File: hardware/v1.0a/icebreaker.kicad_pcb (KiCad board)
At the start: 4 copper layers, 73 x 37 mm, 124 parts, among them J1 Jumper, J10 Jumper, J11 Jumper, J12 Jumper, J13 Jumper, J14 Jumper, J15 Jumper, J16 Jumper, J17 Jumper, J18 Jumper, J19 Jumper, J2 Jumper, J20 Flash, J21 PMOD_1A, J22 PMOD_1B, J23 PMOD_2H, J24 PMOD_2P, J25 RGB Led, J26 5V AUX, J27 5V AUX, J3 Jumper, J4 Jumper, J5 Jumper, J6 Jumper, J7 Jumper, J8 Jumper, J9 Jumper, P1 pkl_USB_OTG, P2 UP, P3 UP, P4 UP, P5 UP, SW1 TACT, SW2 TACT, SW3 TACT, SW4 TACT, U1 93C46B-SOT-23-6, U2 3.3V, U3 1V2, U4 FT2232H, U5 W25Q, U6 ICE5LP4K-SG48, U7 12MHz

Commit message: Use normally closed jumpers. And fix VCCIO2 bypass. Closes #11
These jumpers connect two nets without impacting the schematic net
lists. This is a safer solution and easier to read than having to
remember where the net jumpers have to go and not miss a side path.
These jumpers use a hack of KiCAD where the DRC ignores lines on the
copper layer in footprints. The two pads of the jumper are shorted
within the footprint but they are not from the perspective of the DRC.
While I was already at it I have also replaced / separator with |
separator for multifunction nets. Unfortunately KiCAD reserves the /
separator for its multisheet net naming. This patch should fix the
bypass of the VCCIO0 jumper that was a mistake in the previous versions
of the board.
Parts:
- added REF**: 1b2_Logo_SilkS_5mm, pkl_logos:1b2_Logo_SilkS_5mm, B.Cu at (42.2, 47.2)
- J1, J15, J16, J18, J2: footprint pkl_jumpers:J_0603 -> pkl_jumpers:J_NC_0603_15
- J14, J17, J19: footprint pkl_jumpers:J_0603 -> pkl_jumpers:J_NC_0603_30
- turned J17 to 135 degrees
- turned J19 to 45 degrees
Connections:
- net Net-(C24-Pad1) renamed /VCCPLL
- C23 pad 1: +1V2 -> /VCORE
- C25 pad 1: +1V2 -> /VCORE
- C27 pad 2: +3V3 -> /VCCIO_2
- C28 pad 1: +1V2 -> /VCORE
- C30 pad 1: +3V3 -> /VCCIO_0|1
- C31 pad 1: +3V3 -> /VCCIO_0|1
- C36 pad 1: +1V2 -> /VCORE
- C37 pad 1: +1V2 -> /VCORE
- C38 pad 1: +1V2 -> /VCORE
- J1 pad 1: /Rx_TTL|FIFO_D0 -> /xFIFO_D0
- J14 pad 1: +1V2 -> /VCORE
- J15 pad 2: /FLASH_MOSI|IO0 -> /iCE_MISO
- J16 pad 1: /FLASH_MISO|IO1 -> /iCE_MOSI
- J17 pad 1: +3V3 -> /VCCIO_2
- J18 pad 1: /iCE_SS_B -> /FLASH_CS
- J19 pad 1: +3V3 -> /VCCIO_0|1
- J2 pad 1: /Tx_TTL|FIFO_D1 -> /xFIFO_D1
- J20 pad 1: /iCE_SS_B -> /FLASH_CS
- R10 pad 2: +1V2 -> /VCORE
- R11 pad 6: /iCE_SS_B -> /FLASH_CS
- U4 pad 38: /Rx_TTL|FIFO_D0 -> /xFIFO_D0
- U4 pad 39: /Tx_TTL|FIFO_D1 -> /xFIFO_D1
- U5 pad 1: /iCE_SS_B -> /FLASH_CS
- U6 pad 1: +3V3 -> /VCCIO_2
- U6 pad 14: /FLASH_MOSI|IO0 -> /iCE_MISO
- U6 pad 17: /FLASH_MISO|IO1 -> /iCE_MOSI
- U6 pad 22: +3V3 -> /VCCIO_0|1
- U6 pad 30: +1V2 -> /VCORE
- U6 pad 33: +3V3 -> /VCCIO_0|1
- U6 pad 5: +1V2 -> /VCORE
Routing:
- net +1V2: track 47.5 -> 18.4 mm, vias 4 -> 1
- net /VCORE: track 0.00 -> 27.9 mm, vias 0 -> 3
- net /iCE_SS_B: track 61.4 -> 34.5 mm, vias 3 -> 2
- net /FLASH_CS: track 0.00 -> 25.8 mm, vias 0 -> 1
- net +3V3: track 94.7 -> 69.5 mm, vias 35 -> 32
- net /VCCIO_0|1: track 0.00 -> 18.3 mm, vias 0 -> 2
- net /Rx_TTL|FIFO_D0: track 19.6 -> 7.27 mm, vias 2 -> 1
- net /xFIFO_D0: track 0.00 -> 11.1 mm, vias 0 -> 1
- net /FLASH_MISO|IO1: track 51.3 -> 40.2 mm, vias 3 -> 2
- net /FLASH_MOSI|IO0: track 51.4 -> 40.4 mm, vias 3 -> 2
- net /iCE_MOSI: track 0.00 -> 9.90 mm, vias 0 -> 1
- net /iCE_MISO: track 0.00 -> 9.79 mm, vias 0 -> 1
- net /Tx_TTL|FIFO_D1: track 17.7 -> 9.84 mm, vias 2 -> 1
- net /xFIFO_D1: track 0.00 -> 6.70 mm, vias 0 -> 1
- net /VCCIO_2: track 0.00 -> 4.55 mm, vias 0 -> 1

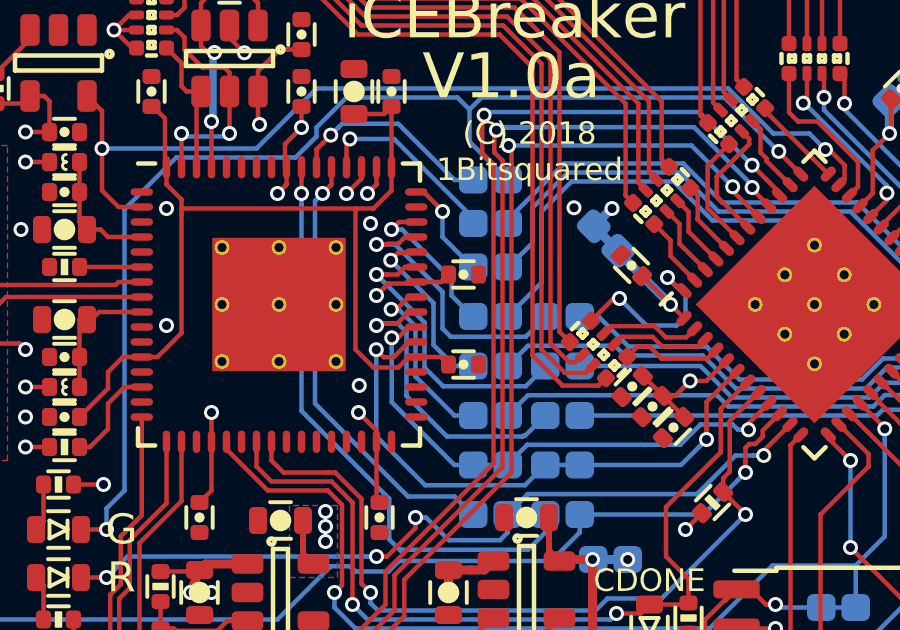
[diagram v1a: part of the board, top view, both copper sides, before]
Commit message: Added pulldown on the B port ~CTS ftdi line. Closes #10
With this line pulled down we can use minicom even when hardware flow
control is enabled. If this pin is not pulled low and hardware flow
control is used, no data is ever sent out by the FTDI chip. This can
easily happen because minicom has hardware flow control enabled by
default.

I decided to only add the CTS line pulldown to keep the placements under
control.
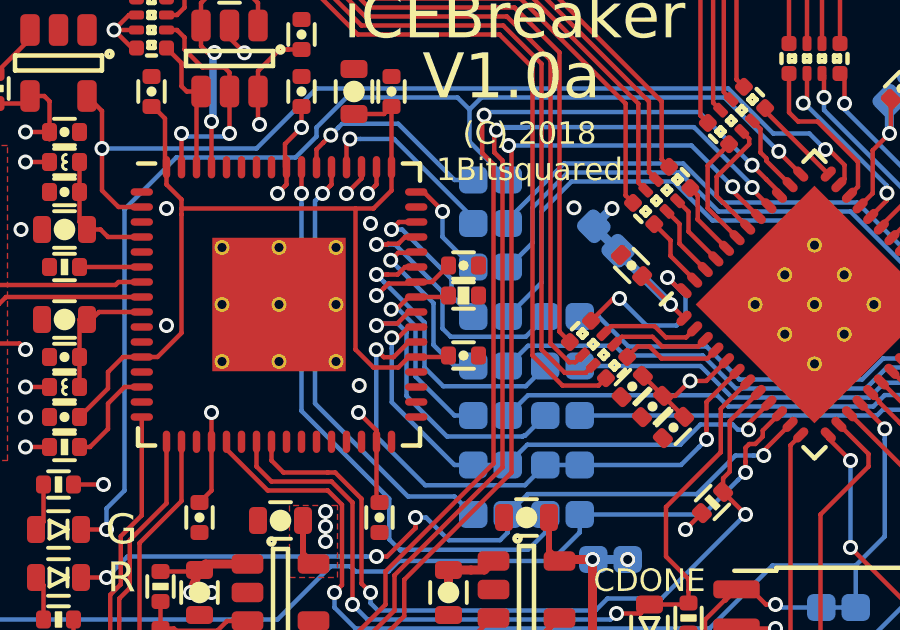
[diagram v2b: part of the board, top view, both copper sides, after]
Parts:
- added R25: 10k, pkl_dipol:R_0402, F.Cu at (50.5, 47.2)
- moved C16 0.30 mm to (50.5, 49.2)
- moved C20 0.30 mm to (50.5, 46.2)
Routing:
- net /xFIFO_D3: track 6.19 -> 7.29 mm
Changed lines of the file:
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@@
     (thickness 1.6)
     (drawings 143)
-    (tracks 1396)
+    (tracks 1398)
     (zones 0)
-    (modules 125)
+    (modules 126)
     (nets 133)
   )
@@
     (add_net "Net-(U7-Pad2)")
   )
+  (module pkl_dipol:R_0402 (layer F.Cu)
+    (at 50.5 47.2)
+    (descr "Resistor SMD 0402, reflow soldering")
+    (tags "resistor 0402")
+    (attr smd)
+    (fp_text reference R25 (at 0 0) (layer F.Fab)
+      (effects (font (size 0.635 0.635) (thickness 0.1)))
+    )
+    (fp_text value 10k (at 1.9 0) (layer F.Fab)
+      (effects (font (size 0.635 0.635) (thickness 0.1)))
+    )
+    (fp_poly (pts (xy -0.175 0.275) (xy -0.175 -0.275) (xy 0.175 -0.275) (xy 0.175 0.275)
+      (xy -0.1 0.275)) (layer F.SilkS) (width 0.05))
+    (fp_line (start -0.95 -0.5) (end 0.95 -0.5) (layer F.CrtYd) (width 0.05))
+    (fp_line (start -0.95 0.5) (end 0.95 0.5) (layer F.CrtYd) (width 0.05))
+    (fp_line (start -0.95 -0.5) (end -0.95 0.5) (layer F.CrtYd) (width 0.05))
+    (fp_line (start 0.95 -0.5) (end 0.95 0.5) (layer F.CrtYd) (width 0.05))
+    (fp_line (start -0.35 -0.44) (end 0.35 -0.44) (layer F.SilkS) (width 0.13))
+    (fp_line (start 0.35 0.44) (end -0.35 0.44) (layer F.SilkS) (width 0.13))
+    (pad 1 smd roundrect (at -0.5 0) (size 0.5 0.6) (layers F.Cu F.Paste F.Mask) (roundrect_rratio 0.25)
+      (net 21 /xFIFO_D3))
+    (pad 2 smd roundrect (at 0.5 0) (size 0.5 0.6) (layers F.Cu F.Paste F.Mask) (roundrect_rratio 0.25)
+      (net 26 GND))
+    (model ${KISYS3DMOD}/Resistor_SMD.3dshapes/R_0402_1005Metric.step
+      (at (xyz 0 0 0))
+      (scale (xyz 1 1 1))
+      (rotate (xyz 0 0 0))
+    )
+  )
   (module pkl_jumpers:J_NC_0603_15 (layer B.Cu)
     (at 53.8 52.85)
@@
   )
   (module pkl_dipol:C_0402 (layer F.Cu)
-    (at 50.5 49.5)
+    (at 50.5 49.2)
     (descr "Capacitor SMD 0402, reflow soldering")
     (tags "capacitor 0402")
@@
       (effects (font (size 0.635 0.635) (thickness 0.1)))
     )
-    (fp_text value 100n (at 0.2 1.2) (layer F.Fab)
+    (fp_text value 100n (at 0.2 1) (layer F.Fab)
       (effects (font (size 0.635 0.635) (thickness 0.1)))
     )
-    (fp_circle (center 0 0) (end 0 -0.085) (layer F.SilkS) (width 0.17))
-    (fp_line (start -0.95 -0.5) (end 0.95 -0.5) (layer F.CrtYd) (width 0.05))
-    (fp_line (start -0.95 0.5) (end 0.95 0.5) (layer F.CrtYd) (width 0.05))
-    (fp_line (start -0.95 -0.5) (end -0.95 0.5) (layer F.CrtYd) (width 0.05))
-    (fp_line (start 0.95 -0.5) (end 0.95 0.5) (layer F.CrtYd) (width 0.05))
-    (fp_line (start -0.35 -0.44) (end 0.35 -0.44) (layer F.SilkS) (width 0.13))
     (fp_line (start 0.35 0.44) (end -0.35 0.44) (layer F.SilkS) (width 0.13))
-    (pad 1 smd roundrect (at -0.5 0) (size 0.5 0.6) (layers F.Cu F.Paste F.Mask) (roundrect_rratio 0.25)
-      (net 39 +1V8))
+    (fp_line (start -0.35 -0.44) (end 0.35 -0.44) (layer F.SilkS) (width 0.13))
+    (fp_line (start 0.95 -0.5) (end 0.95 0.5) (layer F.CrtYd) (width 0.05))
+    (fp_line (start -0.95 -0.5) (end -0.95 0.5) (layer F.CrtYd) (width 0.05))
+    (fp_line (start -0.95 0.5) (end 0.95 0.5) (layer F.CrtYd) (width 0.05))
+    (fp_line (start -0.95 -0.5) (end 0.95 -0.5) (layer F.CrtYd) (width 0.05))
+    (fp_circle (center 0 0) (end 0 -0.085) (layer F.SilkS) (width 0.17))
     (pad 2 smd roundrect (at 0.5 0) (size 0.5 0.6) (layers F.Cu F.Paste F.Mask) (roundrect_rratio 0.25)
       (net 26 GND))
+    (pad 1 smd roundrect (at -0.5 0) (size 0.5 0.6) (layers F.Cu F.Paste F.Mask) (roundrect_rratio 0.25)
+      (net 39 +1V8))
     (model ${KISYS3DMOD}/Capacitor_SMD.3dshapes/C_0402_1005Metric.step
       (at (xyz 0 0 0))
@@
   )
   (module pkl_dipol:C_0402 (layer F.Cu)
-    (at 50.5 46.5)
+    (at 50.5 46.2)
     (descr "Capacitor SMD 0402, reflow soldering")
     (tags "capacitor 0402")
@@
       (effects (font (size 0.635 0.635) (thickness 0.1)))
     )
-    (fp_text value 100n (at 0.2 1) (layer F.Fab)
+    (fp_text value 100n (at 2.2 0) (layer F.Fab)
       (effects (font (size 0.635 0.635) (thickness 0.1)))
     )
-    (fp_circle (center 0 0) (end 0 -0.085) (layer F.SilkS) (width 0.17))
-    (fp_line (start -0.95 -0.5) (end 0.95 -0.5) (layer F.CrtYd) (width 0.05))
-    (fp_line (start -0.95 0.5) (end 0.95 0.5) (layer F.CrtYd) (width 0.05))
-    (fp_line (start -0.95 -0.5) (end -0.95 0.5) (layer F.CrtYd) (width 0.05))
-    (fp_line (start 0.95 -0.5) (end 0.95 0.5) (layer F.CrtYd) (width 0.05))
-    (fp_line (start -0.35 -0.44) (end 0.35 -0.44) (layer F.SilkS) (width 0.13))
     (fp_line (start 0.35 0.44) (end -0.35 0.44) (layer F.SilkS) (width 0.13))
-    (pad 1 smd roundrect (at -0.5 0) (size 0.5 0.6) (layers F.Cu F.Paste F.Mask) (roundrect_rratio 0.25)
-      (net 3 +3V3))
+    (fp_line (start -0.35 -0.44) (end 0.35 -0.44) (layer F.SilkS) (width 0.13))
+    (fp_line (start 0.95 -0.5) (end 0.95 0.5) (layer F.CrtYd) (width 0.05))
+    (fp_line (start -0.95 -0.5) (end -0.95 0.5) (layer F.CrtYd) (width 0.05))
+    (fp_line (start -0.95 0.5) (end 0.95 0.5) (layer F.CrtYd) (width 0.05))
+    (fp_line (start -0.95 -0.5) (end 0.95 -0.5) (layer F.CrtYd) (width 0.05))
+    (fp_circle (center 0 0) (end 0 -0.085) (layer F.SilkS) (width 0.17))
     (pad 2 smd roundrect (at 0.5 0) (size 0.5 0.6) (layers F.Cu F.Paste F.Mask) (roundrect_rratio 0.25)
       (net 26 GND))
+    (pad 1 smd roundrect (at -0.5 0) (size 0.5 0.6) (layers F.Cu F.Paste F.Mask) (roundrect_rratio 0.25)
+      (net 3 +3V3))
     (model ${KISYS3DMOD}/Capacitor_SMD.3dshapes/C_0402_1005Metric.step
       (at (xyz 0 0 0))
@@
   (segment (start 32.4 59.1) (end 33.05 59.1) (width 0.15) (layer F.Cu) (net 3))
   (via (at 33.45 58.7) (size 0.5) (drill 0.3) (layers F.Cu B.Cu) (net 3))
-  (segment (start 49.75 46.75) (end 50 46.5) (width 0.15) (layer F.Cu) (net 3))
-  (segment (start 48.925 46.75) (end 49.75 46.75) (width 0.15) (layer F.Cu) (net 3))
+  (segment (start 49.45 46.75) (end 50 46.2) (width 0.15) (layer F.Cu) (net 3))
+  (segment (start 48.925 46.75) (end 49.45 46.75) (width 0.15) (layer F.Cu) (net 3))
   (segment (start 64.541475 51.998135) (end 64.541475 51.644582) (width 0.15) (layer B.Cu) (net 4))
   (segment (start 64.541475 51.609242) (end 64.541475 51.644582) (width 0.15) (layer F.Cu) (net 4))
@@
   (segment (start 48.925 47.25) (end 48.675 47.25) (width 0.15) (layer F.Cu) (net 21))
   (segment (start 48.675 47.25) (end 48.264647 47.660353) (width 0.15) (layer F.Cu) (net 21))
+  (segment (start 49.95 47.25) (end 50 47.2) (width 0.15) (layer F.Cu) (net 21))
+  (segment (start 48.925 47.25) (end 49.95 47.25) (width 0.15) (layer F.Cu) (net 21))
   (segment (start 49.95 51.9) (end 52.475722 51.9) (width 0.15) (layer B.Cu) (net 22))
   (segment (start 52.550011 51.874989) (end 53.225 51.2) (width 0.15) (layer B.Cu) (net 22))
@@
   (segment (start 37.7 51.25) (end 38.65 50.3) (width 0.15) (layer F.Cu) (net 39))
   (segment (start 39.15 49.25) (end 39.775 49.25) (width 0.15) (layer F.Cu) (net 39))
-  (segment (start 49.75 49.25) (end 50 49.5) (width 0.15) (layer F.Cu) (net 39))
-  (segment (start 48.925 49.25) (end 49.75 49.25) (width 0.15) (layer F.Cu) (net 39))
+  (segment (start 49.95 49.25) (end 50 49.2) (width 0.15) (layer F.Cu) (net 39))
+  (segment (start 48.925 49.25) (end 49.95 49.25) (width 0.15) (layer F.Cu) (net 39))
   (segment (start 38.05 52.25) (end 38.65 51.65) (width 0.15) (layer F.Cu) (net 40))
   (segment (start 38.65 50.8) (end 39.2 50.25) (width 0.15) (layer F.Cu) (net 40))

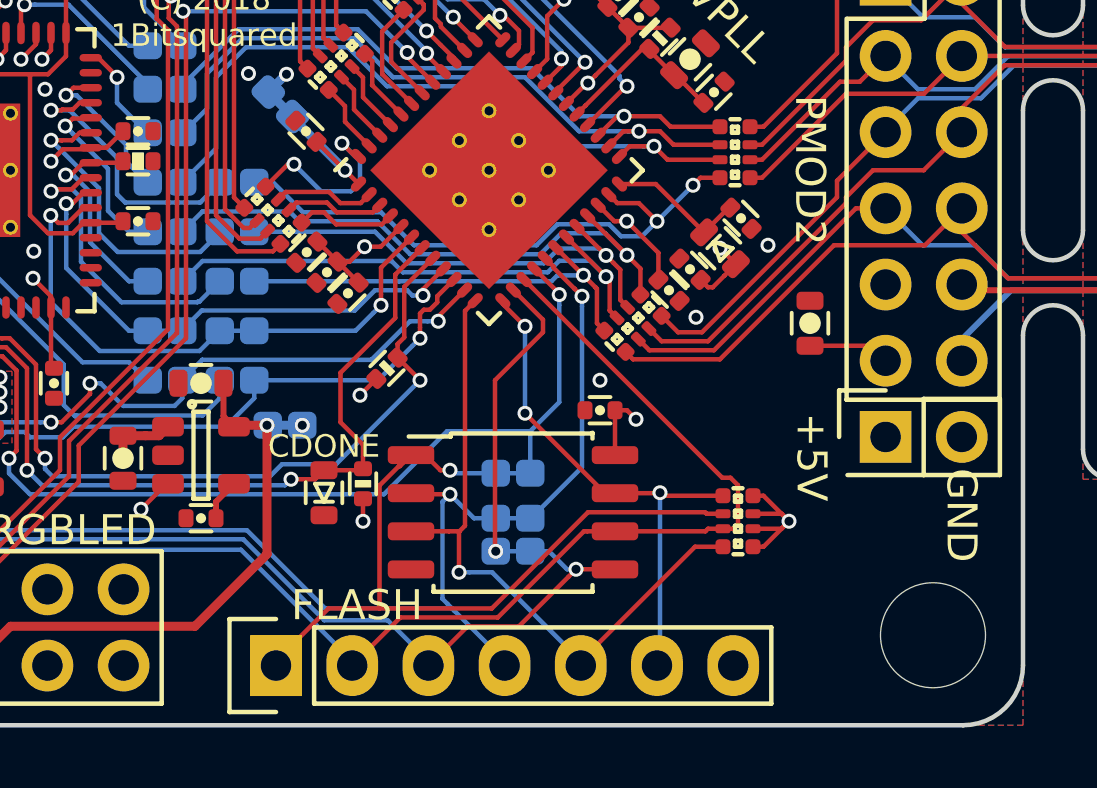
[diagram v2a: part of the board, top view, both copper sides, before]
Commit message: Add an FPGA CRESET jumper. Fixes #9
Adding an in line resistor for the CRESET line from FTDI as well as a
jumper that allows access and pulldown of the CRESET line. This allows
us to override the CRESET signal from FTDI and force the FPGA chip to
stay in reset in cases when we need to access the flash and prevent the
FPGA from configuring the FLASH chip. Especially in cases when the FPGA
is using the FLASH after the design is loaded and configures the flash
into QSPI and other higher bit modes.
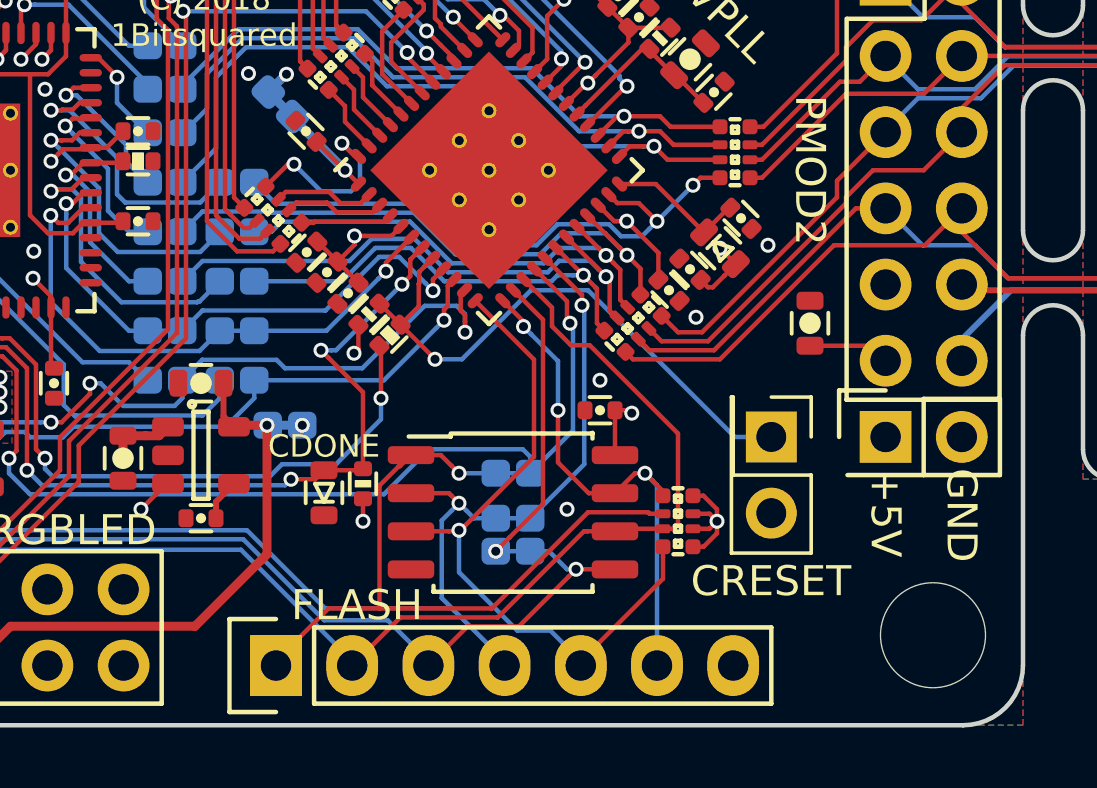
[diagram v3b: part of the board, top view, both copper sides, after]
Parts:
- added J28: CRESET, Connector_PinHeader_2.54mm:PinHeader_2x01_P2.54mm_Vertical, F.Cu at (71.6, 56.4)
- added R26: 10k, pkl_dipol:R_0402, F.Cu at (58.9, 53.0)
- moved R11 2.00 mm to (68.5, 59.2)
- moved R19 1.90 mm to (58.2, 52.3)
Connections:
- U4 pad 24: /iCE_CRESET -> /xiCE_CRESET
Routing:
- net /xiCE_CRESET: track 0.00 -> 22.3 mm, vias 0 -> 2
- net /iCE_CRESET: track 26.5 -> 19.5 mm, vias 2 -> 1
- net /iCE_SCK: track 55.8 -> 53.2 mm
- net /~LEDR: track 27.0 -> 29.2 mm
- net /FLASH_CS: track 25.8 -> 23.8 mm
- net +3V3: track 69.6 -> 68.5 mm
- net /P2_10: track 14.5 -> 15.4 mm
- net /Tx_TTL|FIFO_D1: track 9.84 -> 10.7 mm
- net /iCE_CDONE: track 28.4 -> 29.2 mm, vias 2 -> 4
- net /iCE_SS_B: track 34.5 -> 35.3 mm
- net /P2_4: track 18.3 -> 18.9 mm
- net /VCORE: track 27.9 -> 28.5 mm
- net /Rx_TTL|FIFO_D0: track 7.27 -> 6.70 mm
- net GND: vias 22 -> 23

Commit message: Silkscreen improvements.
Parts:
- moved R11 6.94 mm to (62.9, 55.1), turned to 270 degrees
- moved J27 2.54 mm to (75.4, 58.9)
- moved J28 1.27 mm to (70.3, 56.4)
- moved C34 0.30 mm to (73.2, 52.6), turned to 0 degrees
- moved C32 0.18 mm to (48.7, 35.8), turned to 90 degrees
- moved C33 0.15 mm to (71.6, 35.8), turned to 90 degrees
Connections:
- net /iCE_MISO renamed /iCE_SO
- net /iCE_MOSI renamed /iCE_SI
- R11 pad 2: /FLASH_~WP~|IO2 -> /FLASH_~HLD~|~RST~|IO3
- R11 pad 8: /FLASH_~HLD~|~RST~|IO3 -> /FLASH_~WP~|IO2
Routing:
- net /FLASH_CS: track 23.8 -> 15.1 mm, vias 1 -> 2
- net /FLASH_~WP~|IO2: track 23.1 -> 16.8 mm
- net /iCE_SCK: track 53.2 -> 59.4 mm
- net /FLASH_~HLD~|~RST~|IO3: track 17.3 -> 22.4 mm, vias 3 -> 1
- net +5V: track 147.2 -> 144.7 mm
- net Net-(R6-Pad1): track 8.67 -> 6.47 mm
- net +3V3: track 68.5 -> 67.2 mm
- net /iCE_CRESET: track 19.5 -> 18.3 mm
- net /iCE_SS_B: track 35.3 -> 36.1 mm
- net /iCE_SI: track 9.95 -> 10.5 mm
- net GND: vias 23 -> 21
- net (no net): vias 0 -> 1
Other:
- board text added: "CRESET"
